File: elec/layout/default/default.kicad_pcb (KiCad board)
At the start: 2 copper layers, 77 parts, among them U10 1kΩ ±1% 62.5mW, U11 1kΩ ±1% 62.5mW, U12 1kΩ ±1% 62.5mW, U13 1kΩ ±1% 62.5mW, U14 1kΩ ±1% 62.5mW, U15 1kΩ ±1% 62.5mW, U16 1kΩ ±1% 62.5mW, U17 1kΩ ±1% 62.5mW, U18 1kΩ ±1% 62.5mW, U7 1kΩ ±1% 62.5mW, U8 1kΩ ±1% 62.5mW, U9 1kΩ ±1% 62.5mW

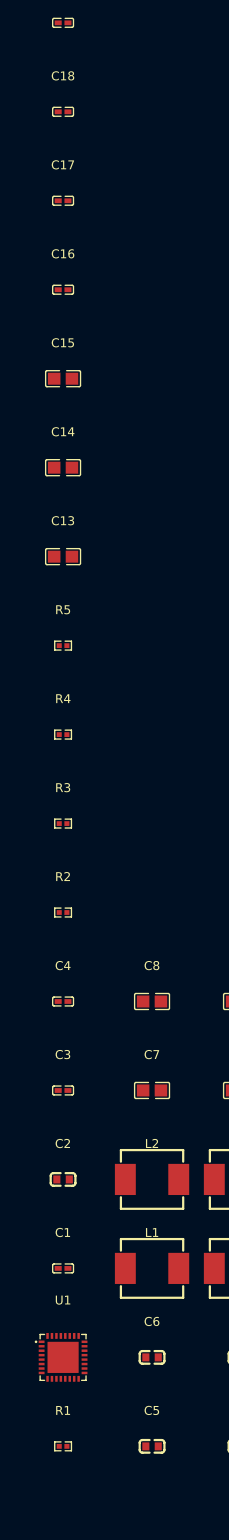
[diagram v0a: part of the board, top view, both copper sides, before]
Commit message: update usb connector
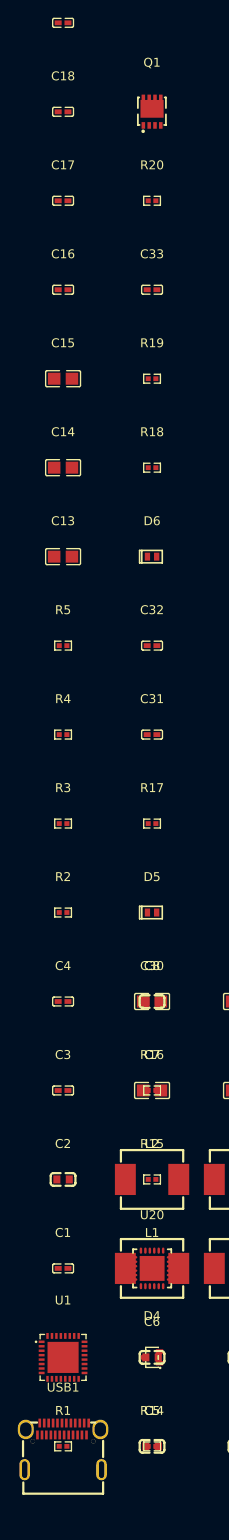
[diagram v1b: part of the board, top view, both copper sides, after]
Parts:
- added C30: 4.7µF ±10% 35V X5R, Murata_Electronics_GRM188R6YA475KE15D:C0603, F.Cu at (10.0, -50.0)
- added C31: 1µF ±10% 25V X5R, Samsung_Electro_Mechanics_CL05A105KA5NQNC:C0402, F.Cu at (10.0, -80.0)
- added C32: 1µF ±10% 25V X5R, Samsung_Electro_Mechanics_CL05A105KA5NQNC:C0402, F.Cu at (10.0, -90.0)
- added C33: 100nF ±10% 16V X7R, Samsung_Electro_Mechanics_CL05B104KO5NNNC:C0402, F.Cu at (10.0, -130.0)
- added D4: , STMicroelectronics_ESDA25W:SOT-323-3_L2.1-W1.3-P1.32-LS2.1-BR, F.Cu at (10.0, -10.0)
- added D5: , STMicroelectronics_ESDA25P35_1U1M:DFN1610-2_L1.6-W1.0-P1.05-RD, F.Cu at (10.0, -60.0)
- added D6: , STMicroelectronics_ESDA25P35_1U1M:DFN1610-2_L1.6-W1.0-P1.05-RD, F.Cu at (10.0, -100.0)
- added Q1: , ALLPOWER_AP30P30Q:PDFN3333-8_L3.1-W3.2-P0.65-LS3.4-BL, F.Cu at (10.0, -150.0)
- added R14: 1kΩ ±1% 62.5mW, UNI_ROYAL_0402WGF1001TCE:R0402, F.Cu at (10.0, 0.00)
- added R15: 4.7kΩ ±1% 62.5mW, UNI_ROYAL_0402WGF4701TCE:R0402, F.Cu at (10.0, -30.0)
- added R16: 4.7kΩ ±1% 62.5mW, UNI_ROYAL_0402WGF4701TCE:R0402, F.Cu at (10.0, -40.0)
- added R17: 1kΩ ±1% 62.5mW, UNI_ROYAL_0402WGF1001TCE:R0402, F.Cu at (10.0, -70.0)
- added R18: 100kΩ ±1% 62.5mW, UNI_ROYAL_0402WGF1003TCE:R0402, F.Cu at (10.0, -110.0)
- added R19: 22kΩ ±1% 62.5mW, UNI_ROYAL_0402WGF2202TCE:R0402, F.Cu at (10.0, -120.0)
- added R20: 100Ω ±1% 62.5mW, UNI_ROYAL_0402WGF1000TCE:R0402, F.Cu at (10.0, -140.0)
- added U20: , STMicroelectronics_STUSB4500QTR:QFN-24_L4.0-W4.0-P0.50-BL-EP2.8, F.Cu at (10.0, -20.0)
- added USB1: , XKB_Connectivity_U262_241N_4BV64:USB-C-SMD_TYC-324G, F.Cu at (0.00, 0.00)
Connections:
- net SCL renamed line-1
- net SDA renamed line-2

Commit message: debug headers
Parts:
- added U21: , JST_Sales_America_B02B_XASK_1_A_LF__SN:CONN-TH_B02B-XASK-1-A-LF-SN, F.Cu at (0.00, 0.00)
- added U22: , JST_Sales_America_B02B_XASK_1_A_LF__SN:CONN-TH_B02B-XASK-1-A-LF-SN, F.Cu at (0.00, -10.0)
- added U23: , HCTL_HC_TYPE_C_24P_VS9_3_5A_F1_1_04:USB-C-SMD_HC-TYPE-C-24P-VS9.3-5A-F1.1-04, F.Cu at (10.0, 0.00)
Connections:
- net A10 renamed pd_controller.usb_connector-A10
- net A11 renamed pd_controller.usb_connector-A11
- net A2 renamed pd_controller.usb_connector-A2
- net A3 renamed pd_controller.usb_connector-A3
- net A8 renamed pd_controller.usb_connector-A8
- net B10 renamed pd_controller.usb_connector-B10
- net B11 renamed pd_controller.usb_connector-B11
- net B2 renamed pd_controller.usb_connector-B2
- net B3 renamed pd_controller.usb_connector-B3
- net B8 renamed pd_controller.usb_connector-B8
- net SCLK renamed line-3
- net SDIN renamed line-5
- net amplifier-line renamed line-6
- net amplifier-line-1 renamed line-7
- net amplifier-line-2 renamed line-8
- net amplifier-line-3 renamed line-9
- net cm5-pins[28] renamed line-12
- net cm5-pins[49] renamed line-13
- net cm5-pins[50] renamed line-11
- net cm5.cm5-pins[50] renamed pins[50]
- net cm5.cm5.hdi_b-pins[28] renamed pins[28]
- net cm5.cm5.hdi_b-pins[49] renamed pins[49]
- net pd_controller-line renamed A5
- net pd_controller-line-1 renamed B5
- net pins[54] renamed line-10
- CN1 pad 13: LRCLK -> line-1
- CN1 pad 18: line-2 -> line-4
- CN1 pad 83: line-1 -> line-2
- HDR1 pad 2: debug_headers[0]-gnd -> gnd
- HDR1 pad 4: debug_headers[0]-gnd -> gnd
- HDR1 pad 6: debug_headers[0]-gnd -> gnd
- HDR1 pad 8: debug_headers[0]-gnd -> gnd
- HDR2 pad 2: debug_headers[1]-gnd -> gnd
- HDR2 pad 4: debug_headers[1]-gnd -> gnd
- HDR2 pad 6: debug_headers[1]-gnd -> gnd
- HDR2 pad 8: debug_headers[1]-gnd -> gnd
- HDR3 pad 2: debug_headers[2]-gnd -> gnd
- HDR3 pad 4: debug_headers[2]-gnd -> gnd
- HDR3 pad 6: debug_headers[2]-gnd -> gnd
- HDR3 pad 8: debug_headers[2]-gnd -> gnd
- R15 pad 1: line-1 -> line-2
- R16 pad 1: line-2 -> line-4
- U1 pad 12: LRCLK -> line-1
- U1 pad 15: line-2 -> line-4
- U1 pad 16: line-1 -> line-2
- U20 pad 7: line-1 -> line-2
- U20 pad 8: line-2 -> line-4

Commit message: start layout
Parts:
- moved C19 271.8 mm to (139.7, 73.2), turned to -90 degrees
- moved C18 264.9 mm to (149.0, 69.0), turned to -90 degrees
- moved C17 257.3 mm to (150.0, 69.0), turned to -90 degrees
- moved C15 242.9 mm to (151.4, 69.9), turned to -90 degrees
- moved C16 242.4 mm to (138.1, 69.2), turned to -90 degrees
- moved C14 226.0 mm to (136.8, 69.9), turned to -90 degrees
- moved R5 217.6 mm to (143.7, 73.4), turned to -90 degrees
- moved C13 217.0 mm to (135.0, 69.9), turned to -90 degrees
- moved Q1 216.9 mm to (64.6, 60.0)
- moved R4 213.7 mm to (149.4, 72.8)
- moved R20 208.8 mm to (66.7, 60.9), turned to -90 degrees
- moved R3 202.3 mm to (142.7, 73.4), turned to -90 degrees
- moved C33 200.5 mm to (66.2, 62.5), turned to 180 degrees
- moved R13 200.5 mm to (97.9, 59.3), turned to 90 degrees
- moved R2 194.6 mm to (141.7, 73.4), turned to -90 degrees
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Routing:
- net gnd: track 0.00 -> 117.5 mm, vias 0 -> 40
- net cm5-pins[16]: track 0.00 -> 31.3 mm, vias 0 -> 1
- net cm5-pins[14]: track 0.00 -> 27.6 mm, vias 0 -> 1
- net hv-1: track 0.00 -> 25.0 mm, vias 0 -> 9
- net hv: track 0.00 -> 22.4 mm, vias 0 -> 9
- net cm5-pins[9]: track 0.00 -> 21.4 mm, vias 0 -> 1
- net cm5-pins[5]: track 0.00 -> 20.6 mm, vias 0 -> 1
- net cm5-pins[2]: track 0.00 -> 20.3 mm, vias 0 -> 1
- net cm5-pins[4]: track 0.00 -> 19.2 mm, vias 0 -> 1
- net cm5-pins[3]: track 0.00 -> 19.0 mm, vias 0 -> 1
- net cm5-pins[11]: track 0.00 -> 18.3 mm, vias 0 -> 1
- net cm5-pins[8]: track 0.00 -> 16.4 mm, vias 0 -> 1
- net regulator_5v-cathode: track 0.00 -> 16.2 mm
- net OUT_Bpos: track 0.00 -> 15.3 mm
- net cm5-pins[10]: track 0.00 -> 15.0 mm, vias 0 -> 1
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- added copper zone on F.Cu, net (none)
- added copper zone on F.Cu, net OUT_Aneg
- added copper zone on F.Cu, net OUT_Apos
- added copper zone on F.Cu, net OUT_Bneg
- added copper zone on F.Cu, net OUT_Bpos
- added copper zone on F.Cu, net VBUS
- added copper zone on B.Cu, net gnd
- added copper zone on F.Cu, net gnd
- added copper zone on F.Cu, net hv-1
- added copper zone on F.Cu, net hv-2
- added copper zone on F.Cu, net line-6
- added copper zone on F.Cu, net line-7
- added copper zone on F.Cu, net line-8
- added copper zone on F.Cu, net line-9
- added copper zone on F.Cu, net regulator_5v-cathode

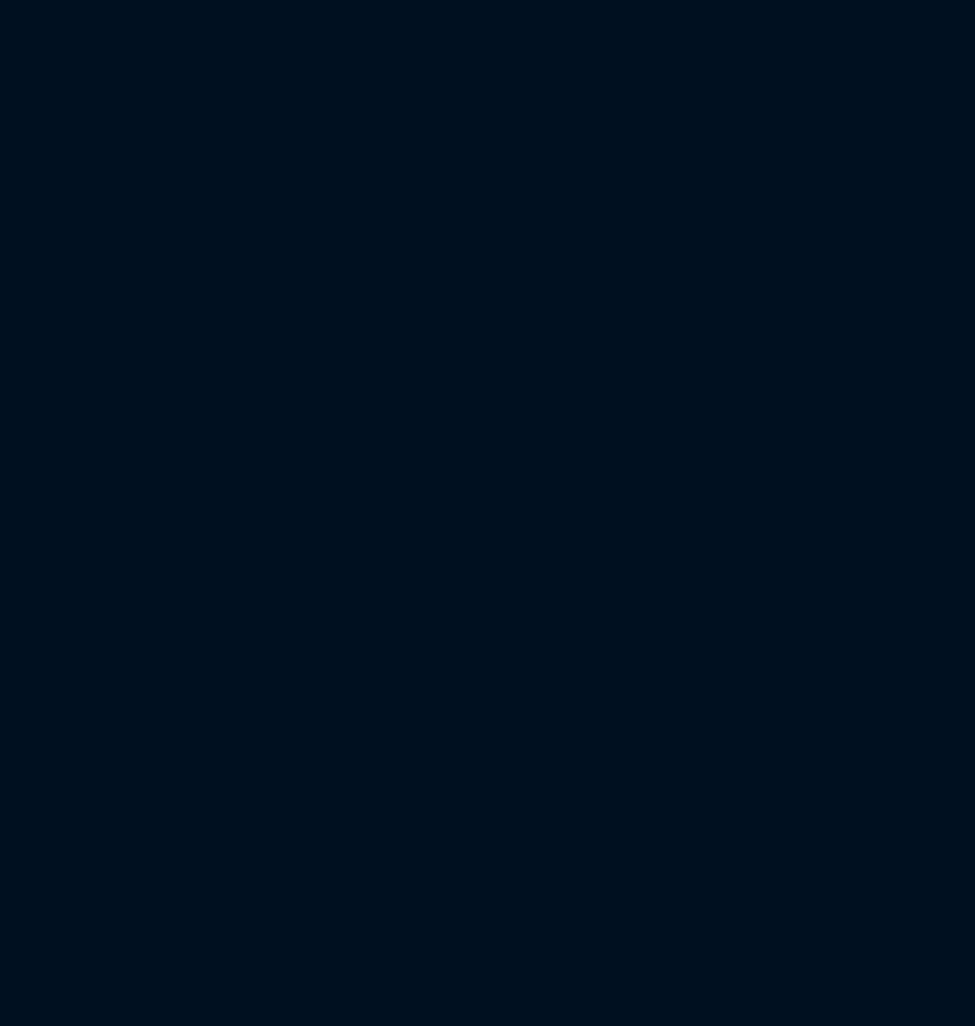
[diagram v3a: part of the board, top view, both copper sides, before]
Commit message: add dsp
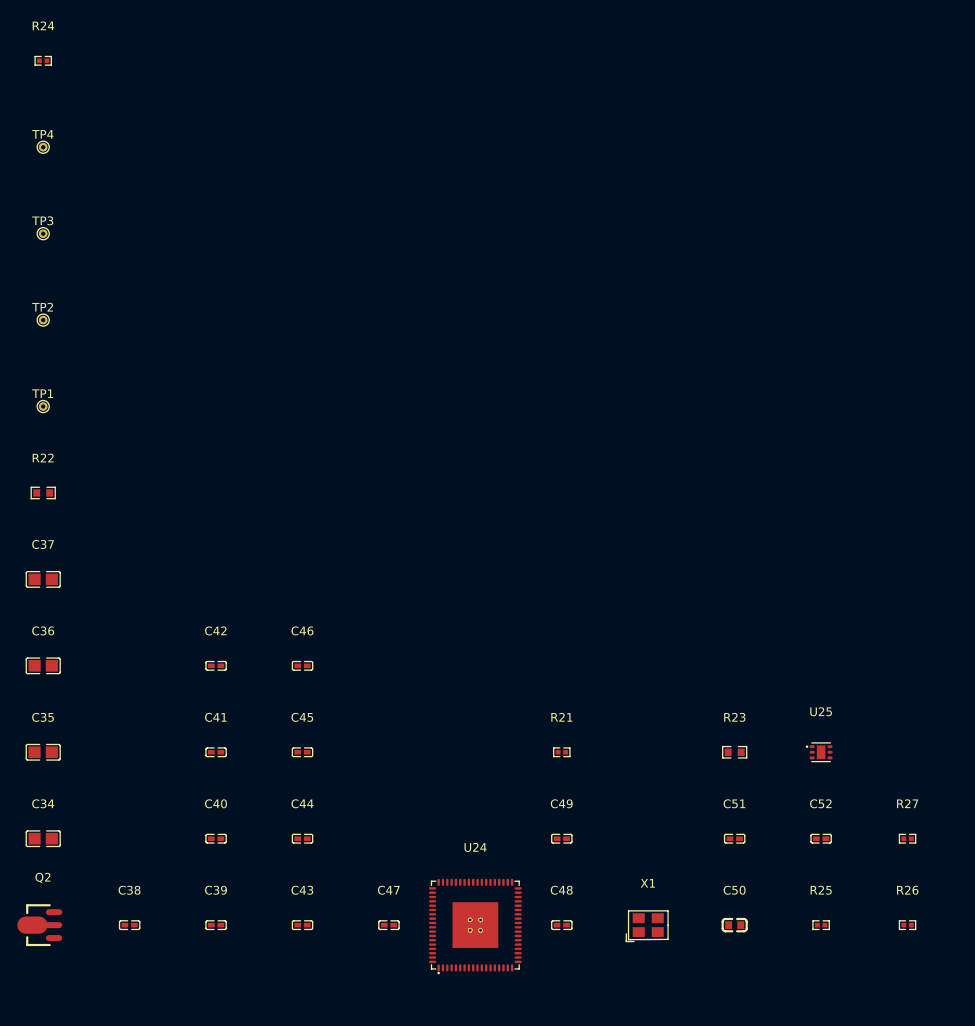
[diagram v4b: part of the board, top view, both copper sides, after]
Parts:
- added C34: 10µF ±10% 25V X5R, Samsung_Electro_Mechanics_CL21A106KAYNNNE:C0805, F.Cu at (0.00, -10.0)
- added C35: 10µF ±10% 25V X5R, Samsung_Electro_Mechanics_CL21A106KAYNNNE:C0805, F.Cu at (0.00, -20.0)
- added C36: 10µF ±10% 25V X5R, Samsung_Electro_Mechanics_CL21A106KAYNNNE:C0805, F.Cu at (0.00, -30.0)
- added C37: 10µF ±10% 25V X5R, Samsung_Electro_Mechanics_CL21A106KAYNNNE:C0805, F.Cu at (0.00, -40.0)
- added C38: 100nF ±10% 16V X7R, Samsung_Electro_Mechanics_CL05B104KO5NNNC:C0402, F.Cu at (10.0, 0.00)
- added C39: 100nF ±10% 16V X7R, Samsung_Electro_Mechanics_CL05B104KO5NNNC:C0402, F.Cu at (20.0, 0.00)
- added C40: 100nF ±10% 16V X7R, Samsung_Electro_Mechanics_CL05B104KO5NNNC:C0402, F.Cu at (20.0, -10.0)
- added C41: 100nF ±10% 16V X7R, Samsung_Electro_Mechanics_CL05B104KO5NNNC:C0402, F.Cu at (20.0, -20.0)
- added C42: 100nF ±10% 16V X7R, Samsung_Electro_Mechanics_CL05B104KO5NNNC:C0402, F.Cu at (20.0, -30.0)
- added C43: 100nF ±10% 16V X7R, Samsung_Electro_Mechanics_CL05B104KO5NNNC:C0402, F.Cu at (30.0, 0.00)
- added C44: 100nF ±10% 16V X7R, Samsung_Electro_Mechanics_CL05B104KO5NNNC:C0402, F.Cu at (30.0, -10.0)
- added C45: 100nF ±10% 16V X7R, Samsung_Electro_Mechanics_CL05B104KO5NNNC:C0402, F.Cu at (30.0, -20.0)
- added C46: 100nF ±10% 16V X7R, Samsung_Electro_Mechanics_CL05B104KO5NNNC:C0402, F.Cu at (30.0, -30.0)
- added C47: 100nF ±10% 16V X7R, Samsung_Electro_Mechanics_CL05B104KO5NNNC:C0402, F.Cu at (40.0, 0.00)
- added C48: 20pF ±5% 50V C0G, YAGEO_CC0402JRNPO9BN200:C0402, F.Cu at (60.0, 0.00)
- added C49: 20pF ±5% 50V C0G, YAGEO_CC0402JRNPO9BN200:C0402, F.Cu at (60.0, -10.0)
- added C50: 5.6nF ±10% 50V X7R, YAGEO_CC0603KRX7R9BB562:C0603, F.Cu at (80.0, 0.00)
- added C51: 150pF ±10% 50V X7R, FH_0402B151K500NT:C0402, F.Cu at (80.0, -10.0)
- added C52: 1µF ±10% 25V X5R, Samsung_Electro_Mechanics_CL05A105KA5NQNC:C0402, F.Cu at (90.0, -10.0)
- added Q2: , Nexperia_PBSS5350X_115:SOT-89-3_L4.5-W2.5-P1.50-LS4.1-TR, F.Cu at (0.00, 0.00)
- added R21: 100Ω ±1% 62.5mW, UNI_ROYAL_0402WGF1000TCE:R0402, F.Cu at (60.0, -20.0)
- added R22: 0Ω 100mW, UNI_ROYAL_0603WAF0000T5E:R0603, F.Cu at (0.00, -50.0)
- added R23: 4.3kΩ ±1% 100mW, UNI_ROYAL_0603WAF4301T5E:R0603, F.Cu at (80.0, -20.0)
- added R24: 1kΩ ±1% 62.5mW, UNI_ROYAL_0402WGF1001TCE:R0402, F.Cu at (0.00, -100.0)
- added R25: 10kΩ ±1% 62.5mW, UNI_ROYAL_0402WGF1002TCE:R0402, F.Cu at (90.0, 0.00)
- added R26: 2kΩ ±1% 62.5mW, UNI_ROYAL_0402WGF2001TCE:R0402, F.Cu at (100.0, 0.00)
- added R27: 10kΩ ±1% 62.5mW, UNI_ROYAL_0402WGF1002TCE:R0402, F.Cu at (100.0, -10.0)
- added TP1: , GENERIC_TESTPOINT:TestPoint_THTPad_D1.0mm_Drill0.5mm, F.Cu at (0.00, -60.0)
- added TP2: , GENERIC_TESTPOINT:TestPoint_THTPad_D1.0mm_Drill0.5mm, F.Cu at (0.00, -70.0)
- added TP3: , GENERIC_TESTPOINT:TestPoint_THTPad_D1.0mm_Drill0.5mm, F.Cu at (0.00, -80.0)
- added TP4: , GENERIC_TESTPOINT:TestPoint_THTPad_D1.0mm_Drill0.5mm, F.Cu at (0.00, -90.0)
- added U24: , Analog_Devices_ADAU1452WBCPZ:LFCSP-72_L10.0-W10.0-P0.50-LS10.2-BL-EP5.3, F.Cu at (50.0, 0.00)
- added U25: , Texas_Instruments_TLV75901PDRVR:WSON-6_L2.0-W2.0-P0.65-TL-EP, F.Cu at (90.0, -20.0)
- added X1: , TAE_TXM12_288M0004322FBCDO00T:CRYSTAL-SMD_4P-L3.2-W2.5-BL-2, F.Cu at (70.0, 0.00)
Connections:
- net EN renamed regulator_5v-EN
- net FB renamed regulator_5v-FB
- C11 pad 1: line-8 -> line-5
- C12 pad 1: line-9 -> line-6
- C7 pad 1: line-6 -> line-3
- C8 pad 1: line-7 -> line-4
- CN1 pad 13: line-1 -> line-12
- CN1 pad 18: line-4 -> line-2
- CN1 pad 25: line-13 -> line-10
- CN1 pad 73: line-10 -> line-7
- CN1 pad 75: line-11 -> line-8
- CN1 pad 76: line-3 -> line-11
- CN1 pad 83: line-2 -> line-1
- CN1 pad 86: line-12 -> line-9
- CN1 pad 88: line-5 -> line-13
- L1 pad 2: line-6 -> line-3
- L2 pad 2: line-7 -> line-4
- L3 pad 2: line-8 -> line-5
- L4 pad 2: line-9 -> line-6
- R15 pad 1: line-2 -> line-1
- R16 pad 1: line-4 -> line-2
- U1 pad 12: line-1 -> LRCLK
- U1 pad 13: line-3 -> SCLK
- U1 pad 14: line-5 -> SDIN
- U1 pad 15: line-4 -> line-2
- U1 pad 16: line-2 -> line-1
- U20 pad 7: line-2 -> line-1
- U20 pad 8: line-4 -> line-2
- U21 pad 1: line-7 -> line-4
- U21 pad 2: line-6 -> line-3
- U22 pad 1: line-9 -> line-6
- U22 pad 2: line-8 -> line-5
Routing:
- net (no net): track 0.00 -> 28.8 mm, vias 0 -> 10
- net hv: track 22.4 -> 0.00 mm, vias 9 -> 0
- net line-8: track 9.14 -> 0.00 mm
- net line-5: track 0.00 -> 9.14 mm
- net line-9: track 9.13 -> 0.00 mm
- net line-3: track 0.00 -> 8.52 mm
- net line-7: track 8.50 -> 0.00 mm
- net line-4: track 4.26 -> 8.50 mm
- net line-2: track 2.17 -> 0.00 mm, vias 1 -> 0
- net line-6: track 8.52 -> 9.13 mm
- added copper zone on F.Cu, net line-3
- added copper zone on F.Cu, net line-4
- added copper zone on F.Cu, net line-5
- removed copper zone on F.Cu, net line-7
- removed copper zone on F.Cu, net line-8
- removed copper zone on F.Cu, net line-9

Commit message: initial placement and cleanup of ato design
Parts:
- added FPC1: , TE_Connectivity_1_2328702_0:FPC-SMD_10P-P0.50_HDGC_0.5K-HX-10PWB, F.Cu at (149.4, 27.2)
- U23: moved to B.Cu
- moved TP4 221.7 mm to (156.0, 67.5)
- moved TP3 221.5 mm to (158.0, 75.2)
- moved R24 218.1 mm to (139.9, 67.4), turned to -90 degrees
- moved TP2 216.0 mm to (158.0, 77.2)
- moved TP1 202.8 mm to (147.0, 79.7)
- moved C37 182.7 mm to (140.5, 76.9), turned to 90 degrees
- moved R22 181.1 mm to (142.4, 61.9)
- moved C34 178.3 mm to (156.1, 76.1), turned to -90 degrees
- moved C35 174.7 mm to (153.4, 63.6)
- moved C36 170.8 mm to (142.9, 63.6), turned to 180 degrees
- moved C42 165.9 mm to (154.6, 66.9), turned to 90 degrees
- moved C41 164.7 mm to (152.6, 77.6)
- moved C38 163.3 mm to (154.6, 75.9), turned to -90 degrees
- moved C46 154.4 mm to (142.1, 76.1), turned to 90 degrees
- moved Q2 152.5 mm to (138.4, 64.0), turned to -90 degrees
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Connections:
- net cm5.cm5.hdi_b-pins[26] renamed pins[26]
- CN1 pad 13: line-12 -> line-7
- CN1 pad 25: line-10 -> line-9
- CN1 pad 29: cm5-pins[57] -> pins[57]
- CN1 pad 73: line-7 -> line-11
- CN1 pad 75: line-8 -> line-12
- CN1 pad 76: line-11 -> line-10
- CN1 pad 86: line-9 -> line-8
- CN1 pad 87: cm5-pins[26] -> nRESET
- U22 pad 1: line-6 -> line-5
- U22 pad 2: line-5 -> line-6
- U24 pad 24: line-10 -> nRESET
- U24 pad 57: line-11 -> line-10
- U24 pad 58: line-12 -> line-7
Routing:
- net hv: track 0.00 -> 49.1 mm, vias 0 -> 12
- net gnd: track 117.5 -> 161.0 mm, vias 40 -> 49
- net (no net): track 28.8 -> 0.00 mm, vias 10 -> 0
- net contact: track 0.00 -> 13.0 mm, vias 0 -> 2
- net VDRIVE: track 0.00 -> 7.82 mm
- net XTALOUT: track 0.00 -> 7.74 mm
- net PLLFILT: track 0.00 -> 6.32 mm
- net nOE: track 0.00 -> 5.21 mm
- net line-2: track 0.00 -> 4.26 mm
- net CLKOUT: track 0.00 -> 3.82 mm
- net cm5.rj45-anode: track 3.36 -> 0.00 mm
- net line-1: track 0.00 -> 2.17 mm, vias 0 -> 1
- net XTALIN_MCLK: track 0.00 -> 1.88 mm
- net regulator_5v-cathode: track 16.2 -> 17.7 mm, vias 0 -> 1
- net dsp.pll_filter-net: track 0.00 -> 1.52 mm
- added copper zone on F.Cu, net collector
- removed copper zone on F.Cu, net line-5
- removed copper zone on F.Cu, net line-6
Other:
- board outline added: 45 x 167 mm
- board text added: "1V2"
- board text added: "2-CH Amplifier"
- board text added: "3V3"
- board text added: "ADAU1452"
- board text added: "CLK"
- board text added: "DSP"
- board text added: "GND"
